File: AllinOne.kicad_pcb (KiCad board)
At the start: 2 copper layers, 268 parts, among them SW0 SW_Push, SW1 SW_Push, SW10 SW_Push, SW100 SW_Push, SW101 SW_Push, SW102 SW_Push, SW103 SW_Push, SW104 SW_Push, SW105 SW_Push, SW106 SW_Push, SW107 SW_Push, SW108 SW_Push, SW109 SW_Push, SW11 SW_Push, SW110 SW_Push, SW111 SW_Push, SW114 SW_Push, SW116 SW_Push, SW117 SW_Push, SW118 SW_Push, SW119 SW_Push, SW12 SW_Push, SW120 SW_Push, SW121 SW_Push, SW122 SW_Push, SW126 SW_Push, SW13 SW_Push, SW130 SW_Push, SW131 SW_Push, SW132 SW_Push, SW133 SW_Push, SW134 SW_Push, SW135 SW_Push, SW136 SW_Push, SW137 SW_Push, SW138 SW_Push, SW139 SW_Push, SW14 SW_Push, SW15 SW_Push, SW16 SW_Push, SW18 SW_Push, SW19 SW_Push, SW2 SW_Push, SW20 SW_Push, SW21 SW_Push, SW22 SW_Push, SW23 SW_Push, SW24 SW_Push, SW25 SW_Push, SW26 SW_Push, SW27 SW_Push, SW28 SW_Push, SW29 SW_Push, SW3 SW_Push, SW30 SW_Push, SW31 SW_Push, SW32 SW_Push, SW33 SW_Push, SW34 SW_Push, SW35 SW_Push, SW36 SW_Push, SW37 SW_Push, SW38 SW_Push, SW39 SW_Push, SW4 SW_Push, SW40 SW_Push, SW41 SW_Push, SW42 SW_Push, SW43 SW_Push, SW44 SW_Push, SW45 SW_Push, SW46 SW_Push, SW47 SW_Push, SW48 SW_Push, SW49 SW_Push, SW5 SW_Push, SW50 SW_Push, SW51 SW_Push, SW52 SW_Push, SW53 SW_Push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

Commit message: Finished wiring rows and columns just needs MCU
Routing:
- net ROW_0: track 0.00 -> 368.9 mm, vias 0 -> 16
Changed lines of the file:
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@@
   (segment (start 350.888 52.630604) (end 350.888 53.467) (width 0.25) (layer "B.Cu") (net 5))
   (segment (start 350.234 45.871) (end 349.309 46.796) (width 0.25) (layer "B.Cu") (net 5))
+  (segment (start 117.540286 97.79) (end 117.561989 97.768297) (width 0.25) (layer "F.Cu") (net 6))
+  (segment (start 175.514 97.79) (end 193.802 97.79) (width 0.25) (layer "F.Cu") (net 6))
+  (segment (start 251.714 97.79) (end 270.002 97.79) (width 0.25) (layer "F.Cu") (net 6))
+  (segment (start 231.902 97.79) (end 250.19 97.79) (width 0.25) (layer "F.Cu") (net 6))
+  (segment (start 137.414 97.79) (end 155.702 97.79) (width 0.25) (layer "F.Cu") (net 6))
+  (segment (start 59.69 97.79) (end 59.563 97.79) (width 0.25) (layer "F.Cu") (net 6))
+  (segment (start 117.583692 97.79) (end 135.89 97.79) (width 0.25) (layer "F.Cu") (net 6))
+  (segment (start 193.802 97.79) (end 211.963 97.79) (width 0.25) (layer "F.Cu") (net 6))
+  (segment (start 79.502 97.79) (end 79.502 95.122) (width 0.25) (layer "F.Cu") (net 6))
+  (segment (start 288.036 97.79) (end 288.163 97.79) (width 0.25) (layer "F.Cu") (net 6))
+  (segment (start 231.902 97.79) (end 231.902 95.122) (width 0.25) (layer "F.Cu") (net 6))
+  (segment (start 211.963 97.79) (end 212.09 97.79) (width 0.25) (layer "F.Cu") (net 6))
+  (segment (start 155.702 97.79) (end 155.702 95.122) (width 0.25) (layer "F.Cu") (net 6))
+  (segment (start 61.214 97.79) (end 79.502 97.79) (width 0.25) (layer "F.Cu") (net 6))
+  (segment (start 117.561989 97.768297) (end 117.583692 97.79) (width 0.25) (layer "F.Cu") (net 6))
+  (segment (start 79.502 97.79) (end 94.458183 97.79) (width 0.25) (layer "F.Cu") (net 6))
+  (segment (start 327.914 97.79) (end 384.302 97.79) (width 0.25) (layer "F.Cu") (net 6))
+  (segment (start 284.752183 97.79) (end 288.036 97.79) (width 0.25) (layer "F.Cu") (net 6))
+  (segment (start 135.89 97.79) (end 135.763 97.79) (width 0.25) (layer "F.Cu") (net 6))
+  (segment (start 308.102 97.79) (end 308.102 95.122) (width 0.25) (layer "F.Cu") (net 6))
+  (segment (start 270.002 97.79) (end 284.752183 97.79) (width 0.25) (layer "F.Cu") (net 6))
+  (segment (start 41.402 95.122) (end 41.402 97.79) (width 0.25) (layer "F.Cu") (net 6))
+  (segment (start 155.702 97.79) (end 173.99 97.79) (width 0.25) (layer "F.Cu") (net 6))
+  (segment (start 94.458183 97.79) (end 97.79 97.79) (width 0.25) (layer "F.Cu") (net 6))
+  (segment (start 41.402 97.79) (end 59.69 97.79) (width 0.25) (layer "F.Cu") (net 6))
+  (segment (start 193.802 97.79) (end 193.802 95.122) (width 0.25) (layer "F.Cu") (net 6))
+  (segment (start 289.56 97.79) (end 308.102 97.79) (width 0.25) (layer "F.Cu") (net 6))
+  (segment (start 384.302 97.79) (end 384.302 95.122) (width 0.25) (layer "F.Cu") (net 6))
+  (segment (start 99.314 97.79) (end 117.540286 97.79) (width 0.25) (layer "F.Cu") (net 6))
+  (segment (start 308.102 97.79) (end 326.39 97.79) (width 0.25) (layer "F.Cu") (net 6))
+  (segment (start 117.554 97.760308) (end 117.554 95.122) (width 0.25) (layer "F.Cu") (net 6))
+  (segment (start 213.614 97.79) (end 231.902 97.79) (width 0.25) (layer "F.Cu") (net 6))
+  (segment (start 117.561989 97.768297) (end 117.554 97.760308) (width 0.25) (layer "F.Cu") (net 6))
+  (segment (start 270.002 97.79) (end 270.002 95.122) (width 0.25) (layer "F.Cu") (net 6))
+  (via (at 211.963 97.79) (size 0.8) (drill 0.4) (layers "F.Cu" "B.Cu") (net 6))
+  (via (at 61.214 97.79) (size 0.8) (drill 0.4) (layers "F.Cu" "B.Cu") (net 6))
+  (via (at 173.99 97.79) (size 0.8) (drill 0.4) (layers "F.Cu" "B.Cu") (net 6))
+  (via (at 99.314 97.79) (size 0.8) (drill 0.4) (layers "F.Cu" "B.Cu") (net 6))
+  (via (at 288.036 97.79) (size 0.8) (drill 0.4) (layers "F.Cu" "B.Cu") (net 6))
+  (via (at 97.79 97.79) (size 0.8) (drill 0.4) (layers "F.Cu" "B.Cu") (net 6))
+  (via (at 59.69 97.79) (size 0.8) (drill 0.4) (layers "F.Cu" "B.Cu") (net 6))
+  (via (at 289.56 97.79) (size 0.8) (drill 0.4) (layers "F.Cu" "B.Cu") (net 6))
+  (via (at 251.714 97.79) (size 0.8) (drill 0.4) (layers "F.Cu" "B.Cu") (net 6))
+  (via (at 250.19 97.79) (size 0.8) (drill 0.4) (layers "F.Cu" "B.Cu") (net 6))
+  (via (at 135.89 97.79) (size 0.8) (drill 0.4) (layers "F.Cu" "B.Cu") (net 6))
+  (via (at 137.414 97.79) (size 0.8) (drill 0.4) (layers "F.Cu" "B.Cu") (net 6))
+  (via (at 213.614 97.79) (size 0.8) (drill 0.4) (layers "F.Cu" "B.Cu") (net 6))
+  (via (at 175.514 97.79) (size 0.8) (drill 0.4) (layers "F.Cu" "B.Cu") (net 6))
+  (via (at 327.914 97.79) (size 0.8) (drill 0.4) (layers "F.Cu" "B.Cu") (net 6))
+  (via (at 326.39 97.79) (size 0.8) (drill 0.4) (layers "F.Cu" "B.Cu") (net 6))
+  (segment (start 61.214 97.79) (end 60.96 97.79) (width 0.25) (layer "B.Cu") (net 6))
+  (segment (start 59.69 97.79) (end 61.214 97.79) (width 0.25) (layer "B.Cu") (net 6))
+  (segment (start 175.514 97.79) (end 175.26 97.79) (width 0.25) (layer "B.Cu") (net 6))
+  (segment (start 251.714 97.79) (end 251.587 97.79) (width 0.25) (layer "B.Cu") (net 6))
+  (segment (start 137.414 97.79) (end 137.16 97.79) (width 0.25) (layer "B.Cu") (net 6))
+  (segment (start 288.036 97.79) (end 289.56 97.79) (width 0.25) (layer "B.Cu") (net 6))
+  (segment (start 326.39 97.79) (end 327.914 97.79) (width 0.25) (layer "B.Cu") (net 6))
+  (segment (start 327.914 97.79) (end 327.787 97.79) (width 0.25) (layer "B.Cu") (net 6))
+  (segment (start 135.89 97.79) (end 137.414 97.79) (width 0.25) (layer "B.Cu") (net 6))
+  (segment (start 250.19 97.79) (end 251.714 97.79) (width 0.25) (layer "B.Cu") (net 6))
+  (segment (start 99.314 97.79) (end 99.06 97.79) (width 0.25) (layer "B.Cu") (net 6))
+  (segment (start 173.99 97.79) (end 175.514 97.79) (width 0.25) (layer "B.Cu") (net 6))
+  (segment (start 211.963 97.79) (end 213.614 97.79) (width 0.25) (layer "B.Cu") (net 6))
+  (segment (start 213.614 97.79) (end 213.487 97.79) (width 0.25) (layer "B.Cu") (net 6))
+  (segment (start 97.79 97.79) (end 99.314 97.79) (width 0.25) (layer "B.Cu") (net 6))
+  (segment (start 289.56 97.79) (end 289.433 97.79) (width 0.25) (layer "B.Cu") (net 6))
   (segment (start 327.152 99.06) (end 327.152 95.122) (width 0.25) (layer "F.Cu") (net 7))
   (segment (start 136.652 99.06) (end 174.752 99.06) (width 0.25) (layer "F.Cu") (net 7))

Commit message: Started routing to MCU
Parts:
- moved C1 23.3 mm to (341.2, 81.9)
- moved C6 23.3 mm to (357.0, 70.0)
- moved C7 23.3 mm to (348.4, 70.0)
- moved Y1 23.3 mm to (352.7, 70.0)
- moved C2 23.3 mm to (357.8, 91.3)
- moved C4 23.3 mm to (343.6, 74.0)
- moved R1 23.3 mm to (362.6, 88.3)
- moved R2 23.3 mm to (338.5, 66.9)
- moved R3 23.3 mm to (335.2, 66.9)
- moved R4 23.3 mm to (340.0, 74.0)
- moved SW_R1 23.3 mm to (340.2, 92.8)
- moved U1 23.3 mm to (352.9, 82.4)
- moved USB1 23.3 mm to (337.2, 54.7)
- moved C3 23.3 mm to (362.1, 77.6)
- moved F1 23.3 mm to (330.6, 76.8)
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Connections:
- U1 pad 1: unconnected-(U1-PE6-Pad1) -> COL_5
- U1 pad 10: unconnected-(U1-PB2-Pad10) -> COL_2
- U1 pad 11: unconnected-(U1-PB3-Pad11) -> COL_1
- U1 pad 12: unconnected-(U1-PB7-Pad12) -> COL_0
- U1 pad 8: unconnected-(U1-PB0-Pad8) -> COL_4
- U1 pad 9: unconnected-(U1-PB1-Pad9) -> COL_3
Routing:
- net COL_0: track 247.7 -> 567.6 mm, vias 0 -> 2
- net COL_1: track 228.6 -> 517.7 mm, vias 0 -> 2
- net COL_2: track 209.6 -> 447.8 mm, vias 0 -> 2
- net COL_3: track 228.6 -> 425.3 mm, vias 0 -> 2
- net COL_4: track 209.5 -> 364.6 mm, vias 0 -> 2
- net COL_5: track 228.6 -> 346.5 mm, vias 0 -> 2
- net COL_6: track 179.3 -> 266.0 mm
- net COL_7: track 236.5 -> 269.6 mm
- net Net-(D84-A): track 0.00 -> 7.74 mm
- net Net-(D104-A): track 0.00 -> 7.74 mm

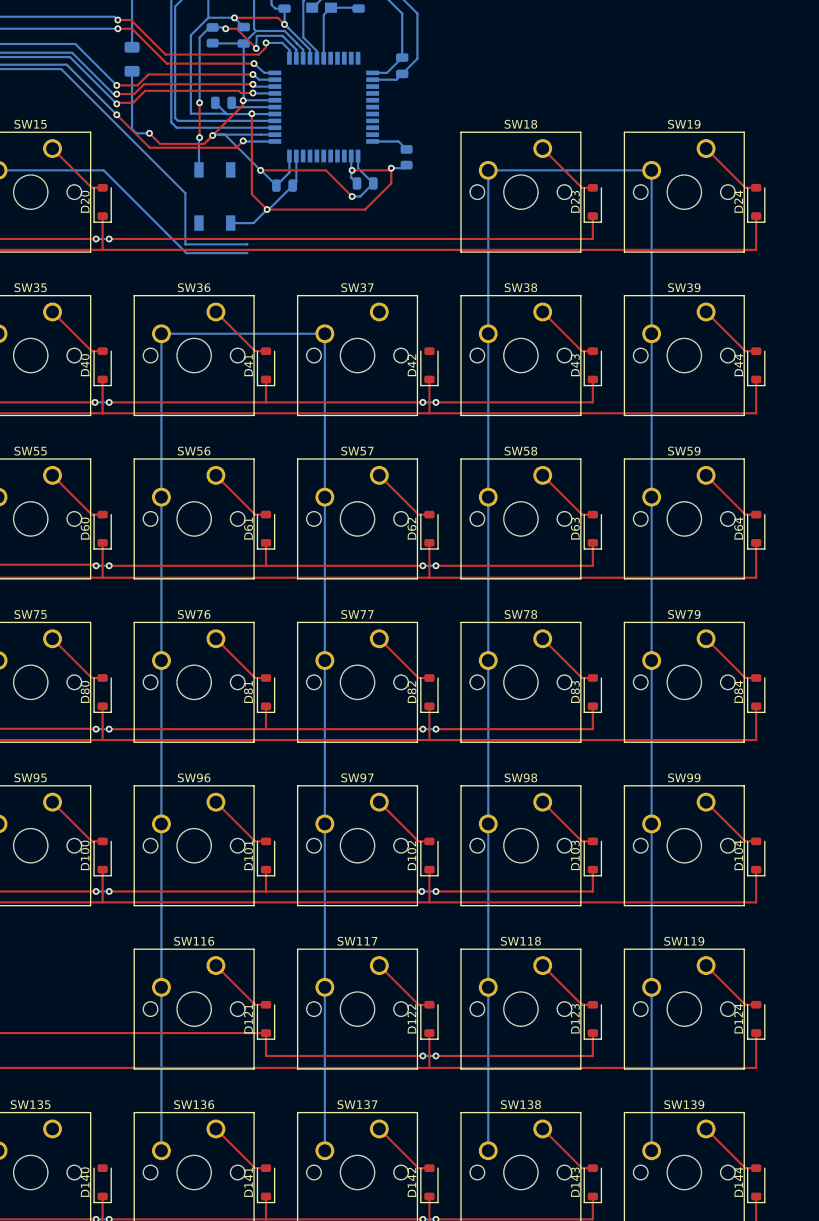
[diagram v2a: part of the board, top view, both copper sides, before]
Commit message: Almost done wiring to the mcu
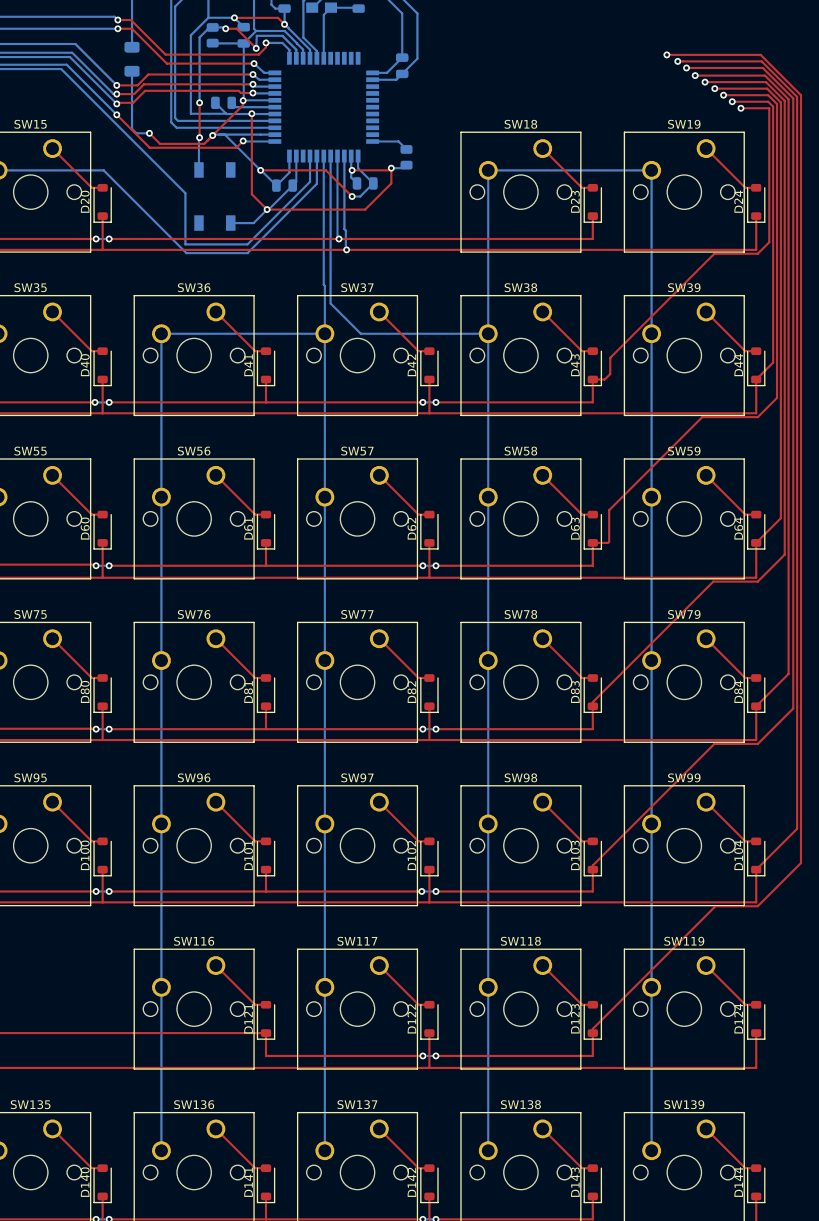
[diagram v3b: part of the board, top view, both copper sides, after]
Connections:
- U1 pad 36: unconnected-(U1-PF7-Pad36) -> ROW_1
- U1 pad 37: unconnected-(U1-PF6-Pad37) -> ROW_0
- U1 pad 38: unconnected-(U1-PF5-Pad38) -> COL_9
- U1 pad 39: unconnected-(U1-PF4-Pad39) -> COL_8
- U1 pad 40: unconnected-(U1-PF1-Pad40) -> COL_7
- U1 pad 41: unconnected-(U1-PF0-Pad41) -> COL_6
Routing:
- net ROW_10: track 365.6 -> 505.5 mm, vias 12 -> 13
- net ROW_8: track 367.9 -> 484.5 mm, vias 16 -> 17
- net ROW_9: track 378.6 -> 486.5 mm, vias 0 -> 1
- net ROW_6: track 371.7 -> 464.9 mm, vias 16 -> 17
- net ROW_7: track 379.1 -> 463.4 mm, vias 0 -> 1
- net ROW_4: track 370.4 -> 442.1 mm, vias 16 -> 17
- net ROW_5: track 379.5 -> 440.5 mm, vias 0 -> 1
- net ROW_2: track 371.5 -> 418.8 mm, vias 18 -> 19
- net ROW_3: track 382.4 -> 420.0 mm, vias 0 -> 1
- net COL_9: track 247.7 -> 284.7 mm
- net COL_8: track 209.6 -> 230.3 mm
- net COL_7: track 269.6 -> 284.2 mm
- net COL_6: track 266.0 -> 279.3 mm
- net ROW_1: track 378.4 -> 389.4 mm, vias 0 -> 1
- net ROW_0: track 368.8 -> 378.8 mm, vias 16 -> 17
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
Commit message: All Done for now
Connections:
- U1 pad 19: unconnected-(U1-PD1-Pad19) -> ROW_13
- U1 pad 20: unconnected-(U1-PD2-Pad20) -> ROW_12
- U1 pad 21: unconnected-(U1-PD3-Pad21) -> ROW_11
- U1 pad 22: unconnected-(U1-PD5-Pad22) -> ROW_10
- U1 pad 25: unconnected-(U1-PD4-Pad25) -> ROW_9
- U1 pad 26: unconnected-(U1-PD6-Pad26) -> ROW_8
- U1 pad 27: unconnected-(U1-PD7-Pad27) -> ROW_7
- U1 pad 28: unconnected-(U1-PB4-Pad28) -> ROW_6
- U1 pad 29: unconnected-(U1-PB5-Pad29) -> ROW_5
- U1 pad 30: unconnected-(U1-PB6-Pad30) -> ROW_4
- U1 pad 31: unconnected-(U1-PC6-Pad31) -> ROW_3
- U1 pad 32: unconnected-(U1-PC7-Pad32) -> ROW_2
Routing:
- net ROW_12: track 365.1 -> 567.7 mm, vias 10 -> 11
- net ROW_13: track 369.7 -> 564.2 mm, vias 0 -> 1
- net ROW_11: track 371.5 -> 541.8 mm, vias 0 -> 1
- net ROW_2: track 418.8 -> 463.1 mm
- net ROW_3: track 420.0 -> 463.2 mm
- net ROW_4: track 442.1 -> 484.7 mm
- net ROW_5: track 440.5 -> 481.6 mm
- net ROW_6: track 464.9 -> 504.9 mm
- net ROW_7: track 463.4 -> 502.2 mm
- net ROW_10: track 505.5 -> 543.5 mm
- net ROW_8: track 484.5 -> 522.3 mm
- net ROW_9: track 486.5 -> 523.2 mm
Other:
- board outline added: 389.9 x 166.2 mm
- board text added: "オリンワーン"
- board text added: "ミゲル"
